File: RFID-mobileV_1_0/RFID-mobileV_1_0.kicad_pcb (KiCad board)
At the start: 2 copper layers, 50.7 x 89.5 mm, 54 parts, among them J1 USB_C_Receptacle_USB2.0, J2 Conn_01x05_Male, J3 Conn_01x05_Female, J4 Conn_01x05_Male, Q1 MMBT3904, SW1 SW_Push, U1 XC6206P332MR, U2 E22-400T22S, U3 STM32G030FxP, U4 LM321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

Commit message: pcb update
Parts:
- moved R13 31.9 mm to (66.3, 142.2), turned to 0 degrees
- moved D1 31.5 mm to (66.3, 144.3), turned to 180 degrees
- moved J4 19.1 mm to (102.6, 84.8), turned to -90 degrees
- moved AE1 3.22 mm to (82.7, 90.9)
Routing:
- net /RFID_RXD_: track 0.00 -> 63.5 mm
- net /RFID_TXD_: track 0.00 -> 61.2 mm
- net /ANT: track 12.2 -> 0.00 mm
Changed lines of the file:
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@@
   (net 55 "unconnected-(U5-Pad1)")
   (footprint "LED_SMD:LED_0805_2012Metric" (layer "F.Cu")
-    (at 90.424 123.952 90)
+    (at 66.294 144.272 180)
     (descr "LED SMD 0805 (2012 Metric), square (rectangular) end terminal, IPC_7351 nominal, (Body size source: https://docs.google.com/spreadsheets/d/1BsfQQcO9C6DZCsRaXUlFlo91Tg2WpOkGARC1WS5S8t0/edit?usp=sharing), generated with kicad-footprint-generator")
     (tags "LED")
@@
     (property "Sheetname" "")
     (attr smd)
-    (fp_text reference "D1" (at 0 -1.65 90) (layer "F.SilkS")
-      (effects (font (size 1 1) (thickness 0.15)))
-    )
-    (fp_text value "PWR" (at 0 1.65 90) (layer "F.Fab")
-      (effects (font (size 1 1) (thickness 0.15)))
-    )
-    (fp_text user "${REFERENCE}" (at 0 0 90) (layer "F.Fab")
+    (fp_text reference "D1" (at 0 -1.65) (layer "F.SilkS")
+      (effects (font (size 1 1) (thickness 0.15)))
+    )
+    (fp_text value "PWR" (at 0 1.65) (layer "F.Fab")
+      (effects (font (size 1 1) (thickness 0.15)))
+    )
+    (fp_text user "${REFERENCE}" (at 0 0) (layer "F.Fab")
       (effects (font (size 0.5 0.5) (thickness 0.08)))
     )
@@
     (fp_line (start 1 0.6) (end 1 -0.6) (layer "F.Fab") (width 0.1))
     (fp_line (start -1 -0.3) (end -1 0.6) (layer "F.Fab") (width 0.1))
-    (pad "1" smd roundrect (at -0.9375 0 90) (size 0.975 1.4) (layers "F.Cu" "F.Paste" "F.Mask") (roundrect_rratio 0.25)
+    (pad "1" smd roundrect (at -0.9375 0 180) (size 0.975 1.4) (layers "F.Cu" "F.Paste" "F.Mask") (roundrect_rratio 0.25)
       (net 7 "GND") (pinfunction "K") (pintype "passive"))
-    (pad "2" smd roundrect (at 0.9375 0 90) (size 0.975 1.4) (layers "F.Cu" "F.Paste" "F.Mask") (roundrect_rratio 0.25)
+    (pad "2" smd roundrect (at 0.9375 0 180) (size 0.975 1.4) (layers "F.Cu" "F.Paste" "F.Mask") (roundrect_rratio 0.25)
       (net 9 "Net-(D1-Pad2)") (pinfunction "A") (pintype "passive"))
     (model "${KICAD6_3DMODEL_DIR}/LED_SMD.3dshapes/LED_0805_2012Metric.wrl"
@@
   )
   (footprint "Resistor_SMD:R_0805_2012Metric" (layer "F.Cu")
-    (at 92.456 123.952 -90)
+    (at 66.294 142.24)
     (descr "Resistor SMD 0805 (2012 Metric), square (rectangular) end terminal, IPC_7351 nominal, (Body size source: IPC-SM-782 page 72, https://www.pcb-3d.com/wordpress/wp-content/uploads/ipc-sm-782a_amendment_1_and_2.pdf), generated with kicad-footprint-generator")
     (tags "resistor")
@@
     (property "Sheetname" "")
     (attr smd)
-    (fp_text reference "R13" (at 0 -1.65 90) (layer "F.SilkS")
-      (effects (font (size 1 1) (thickness 0.15)))
-    )
-    (fp_text value "330" (at 0 1.65 90) (layer "F.Fab")
-      (effects (font (size 1 1) (thickness 0.15)))
-    )
-    (fp_text user "${REFERENCE}" (at 0 0 90) (layer "F.Fab")
+    (fp_text reference "R13" (at 0 -1.65) (layer "F.SilkS")
+      (effects (font (size 1 1) (thickness 0.15)))
+    )
+    (fp_text value "330" (at 0 1.65) (layer "F.Fab")
+      (effects (font (size 1 1) (thickness 0.15)))
+    )
+    (fp_text user "${REFERENCE}" (at 0 0) (layer "F.Fab")
       (effects (font (size 0.5 0.5) (thickness 0.08)))
     )
@@
     (fp_line (start -1 -0.625) (end 1 -0.625) (layer "F.Fab") (width 0.1))
     (fp_line (start -1 0.625) (end -1 -0.625) (layer "F.Fab") (width 0.1))
-    (pad "1" smd roundrect (at -0.9125 0 270) (size 1.025 1.4) (layers "F.Cu" "F.Paste" "F.Mask") (roundrect_rratio 0.243902)
+    (pad "1" smd roundrect (at -0.9125 0) (size 1.025 1.4) (layers "F.Cu" "F.Paste" "F.Mask") (roundrect_rratio 0.243902)
       (net 9 "Net-(D1-Pad2)") (pintype "passive"))
-    (pad "2" smd roundrect (at 0.9125 0 270) (size 1.025 1.4) (layers "F.Cu" "F.Paste" "F.Mask") (roundrect_rratio 0.243902)
+    (pad "2" smd roundrect (at 0.9125 0) (size 1.025 1.4) (layers "F.Cu" "F.Paste" "F.Mask") (roundrect_rratio 0.243902)
       (net 4 "+3V3") (pintype "passive"))
     (model "${KICAD6_3DMODEL_DIR}/Resistor_SMD.3dshapes/R_0805_2012Metric.wrl"
@@
   )
   (footprint "Connector_PinHeader_2.54mm:PinHeader_1x05_P2.54mm_Vertical" (layer "F.Cu")
-    (at 83.566 83.82 90)
+    (at 102.611 84.836 -90)
     (descr "Through hole straight pin header, 1x05, 2.54mm pitch, single row")
     (tags "Through hole pin header THT 1x05 2.54mm single row")
@@
     (fp_line (start 1.27 -1.27) (end 1.27 11.43) (layer "F.Fab") (width 0.1))
     (fp_line (start -1.27 11.43) (end -1.27 -0.635) (layer "F.Fab") (width 0.1))
-    (pad "1" thru_hole rect (at 0 0 90) (size 1.7 1.7) (drill 1) (layers *.Cu *.Mask)
+    (pad "1" thru_hole rect (at 0 0 270) (size 1.7 1.7) (drill 1) (layers *.Cu *.Mask)
       (net 4 "+3V3") (pinfunction "Pin_1") (pintype "passive"))
-    (pad "2" thru_hole oval (at 0 2.54 90) (size 1.7 1.7) (drill 1) (layers *.Cu *.Mask)
+    (pad "2" thru_hole oval (at 0 2.54 270) (size 1.7 1.7) (drill 1) (layers *.Cu *.Mask)
       (net 29 "/RFID_TXD_") (pinfunction "Pin_2") (pintype "passive"))
-    (pad "3" thru_hole oval (at 0 5.08 90) (size 1.7 1.7) (drill 1) (layers *.Cu *.Mask)
+    (pad "3" thru_hole oval (at 0 5.08 270) (size 1.7 1.7) (drill 1) (layers *.Cu *.Mask)
       (net 30 "/RFID_RXD_") (pinfunction "Pin_3") (pintype "passive"))
-    (pad "4" thru_hole oval (at 0 7.62 90) (size 1.7 1.7) (drill 1) (layers *.Cu *.Mask)
+    (pad "4" thru_hole oval (at 0 7.62 270) (size 1.7 1.7) (drill 1) (layers *.Cu *.Mask)
       (net 31 "unconnected-(J4-Pad4)") (pinfunction "Pin_4") (pintype "passive+no_connect"))
-    (pad "5" thru_hole oval (at 0 10.16 90) (size 1.7 1.7) (drill 1) (layers *.Cu *.Mask)
+    (pad "5" thru_hole oval (at 0 10.16 270) (size 1.7 1.7) (drill 1) (layers *.Cu *.Mask)
       (net 7 "GND") (pinfunction "Pin_5") (pintype "passive"))
     (model "${KICAD6_3DMODEL_DIR}/Connector_PinHeader_2.54mm.3dshapes/PinHeader_1x05_P2.54mm_Vertical.wrl"
@@
   )
   (footprint "RF_Antenna:433MHz" (layer "F.Cu")
-    (at 85.852 91.44 180)
+    (at 82.677 90.932001 180)
     (property "Sheetfile" "RFID-mobileV_1_0.kicad_sch")
     (property "Sheetname" "")
@@
   (gr_arc locked (start 66.16277 161.39279) (mid 64.73449 161.282141) (end 64.050435 160.023467) (layer "Edge.Cuts") (width 0.2))
   (gr_circle locked (center 110.407996 100.913642) (end 113.407996 100.913642) (layer "Edge.Cuts") (width 0.2) (fill none))
-  (segment (start 75.692 95.943) (end 75.692 89.154) (width 0.25) (layer "F.Cu") (net 1))
-  (segment (start 75.692 89.154) (end 76.2 88.646) (width 0.25) (layer "F.Cu") (net 1))
-  (segment (start 77.016 97.267) (end 75.692 95.943) (width 0.25) (layer "F.Cu") (net 1))
-  (segment (start 77.016 98.417) (end 77.016 97.267) (width 0.25) (layer "F.Cu") (net 1))
-  (segment (start 76.708 88.646) (end 77.0265 88.9645) (width 0.25) (layer "F.Cu") (net 1))
-  (segment (start 76.2 88.646) (end 76.708 88.646) (width 0.25) (layer "F.Cu") (net 1))
-  (segment (start 77.0265 88.9645) (end 77.0265 89.662) (width 0.25) (layer "F.Cu") (net 1))
   (segment (start 77.216 140.97) (end 79.455 140.97) (width 0.6) (layer "F.Cu") (net 2))
   (segment (start 79.484 140.941) (end 79.455 140.97) (width 0.6) (layer "F.Cu") (net 2))
@@
   (segment (start 101.092 132.842) (end 102.616 134.366) (width 0.25) (layer "F.Cu") (net 28))
   (segment (start 102.616 134.366) (end 102.616 136.144) (width 0.25) (layer "F.Cu") (net 28))
+  (segment (start 105.918 133.35) (end 105.918 113.03) (width 0.25) (layer "F.Cu") (net 29))
+  (segment (start 108.966 111.506) (end 102.616 111.506) (width 0.25) (layer "F.Cu") (net 29))
+  (segment (start 102.616 111.506) (end 100.66256 109.55256) (width 0.25) (layer "F.Cu") (net 29))
+  (segment (start 100.071 94.355282) (end 100.071 84.836) (width 0.25) (layer "F.Cu") (net 29))
+  (segment (start 104.7165 136.013) (end 104.7165 134.5515) (width 0.25) (layer "F.Cu") (net 29))
+  (segment (start 100.66256 94.946842) (end 100.071 94.355282) (width 0.25) (layer "F.Cu") (net 29))
+  (segment (start 105.918 113.03) (end 107.442 111.506) (width 0.25) (layer "F.Cu") (net 29))
+  (segment (start 107.442 111.506) (end 108.966 111.506) (width 0.25) (layer "F.Cu") (net 29))
+  (segment (start 100.66256 109.55256) (end 100.66256 94.946842) (width 0.25) (layer "F.Cu") (net 29))
+  (segment (start 104.7165 134.5515) (end 105.918 133.35) (width 0.25) (layer "F.Cu") (net 29))
+  (segment (start 91.44 134.112) (end 90.05304 132.72504) (width 0.25) (layer "F.Cu") (net 30))
+  (segment (start 90.05304 132.334) (end 100.21304 122.174) (width 0.25) (layer "F.Cu") (net 30))
+  (segment (start 90.05304 132.72504) (end 90.05304 132.334) (width 0.25) (layer "F.Cu") (net 30))
+  (segment (start 100.21304 95.13304) (end 97.531 92.451) (width 0.25) (layer "F.Cu") (net 30))
+  (segment (start 97.0905 134.112) (end 93.726 134.112) (width 0.25) (layer "F.Cu") (net 30))
+  (segment (start 100.21304 122.174) (end 100.21304 120.903999) (width 0.25) (layer "F.Cu") (net 30))
+  (segment (start 93.726 134.112) (end 91.44 134.112) (width 0.25) (layer "F.Cu") (net 30))
+  (segment (start 98.9915 136.013) (end 97.0905 134.112) (width 0.25) (layer "F.Cu") (net 30))
+  (segment (start 97.531 92.451) (end 97.531 84.836) (width 0.25) (layer "F.Cu") (net 30))
+  (segment (start 100.21304 120.903999) (end 100.21304 95.13304) (width 0.25) (layer "F.Cu") (net 30))
   (segment (start 90.756 113.616) (end 88.138 110.998) (width 0.25) (layer "F.Cu") (net 32))
   (segment (start 90.756 114.417) (end 90.756 113.616) (width 0.25) (layer "F.Cu") (net 32))

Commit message: update
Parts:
- AE1: footprint RF_Antenna:433MHz -> RF_Antenna:433MHz_V
- moved R12 19.5 mm to (79.8, 158.5)
- moved C2 18.6 mm to (96.3, 158.0)
- moved C1 18.6 mm to (99.1, 155.2)
- moved U1 18.6 mm to (99.3, 158.0)
- moved U5 18.2 mm to (84.8, 153.9)
- moved J3 13.5 mm to (103.1, 122.2), turned to 0 degrees
- moved C6 11.9 mm to (76.2, 145.0), turned to 90 degrees
- moved BT1 11.8 mm to (78.2, 153.9), turned to 0 degrees
- moved R7 7.55 mm to (79.7, 148.5), turned to 90 degrees
- moved J4 7.27 mm to (104.1, 91.9), turned to 0 degrees
- moved R17 5.99 mm to (88.9, 153.2), turned to 180 degrees
- moved U4 5.85 mm to (79.5, 145.0), turned to 180 degrees
- moved R8 5.64 mm to (81.7, 148.5), turned to -90 degrees
- moved AE1 2.22 mm to (84.8, 90.4)
- moved R11 1.78 mm to (98.6, 164.8), turned to 0 degrees
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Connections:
- D2 pad 1: /PA6 -> /PA8
- D3 pad 1: /PA7 -> /PA9
- D4 pad 1: /PA8 -> /PA10
- U3 pad 12: /VBUS_sing -> /buz
- U3 pad 13: /PA6 -> /VBUS_sing
- U3 pad 16: unconnected-(U3-Pad16) -> /PA9
- U3 pad 17: unconnected-(U3-Pad17) -> /PA10
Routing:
- net +3V3: track 20.7 -> 280.1 mm, vias 0 -> 6
- net +BATT: track 5.78 -> 110.1 mm
- net /buz: track 0.00 -> 81.4 mm
- net /VBUS_sing: track 0.00 -> 45.0 mm
- net /CHAR_STAT: track 0.00 -> 35.8 mm, vias 0 -> 2
- net +5V: track 0.00 -> 33.1 mm
- net /BATT_moint: track 0.00 -> 30.8 mm, vias 0 -> 2
- net /RFID_TXD_: track 61.2 -> 46.2 mm
- net /PA6: track 13.1 -> 0.00 mm
- net /PA9: track 0.00 -> 10.4 mm, vias 0 -> 2
- net /PA7: track 9.93 -> 0.00 mm, vias 2 -> 0
- net /PA10: track 0.00 -> 9.08 mm, vias 0 -> 2
- net /RFID_RXD_: track 63.5 -> 54.9 mm
- net /CC1: track 0.00 -> 8.49 mm
- net /CC2: track 0.00 -> 7.78 mm
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- added copper zone on B.Cu, net GND
- added copper zone on F.Cu, net GND

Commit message: update
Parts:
- moved Q1 2.05 mm to (68.8, 118.1)
- moved R5 2.05 mm to (68.8, 115.1)
- moved R6 2.05 mm to (72.6, 118.1)
- moved R11 1.78 mm to (96.8, 164.8), turned to 180 degrees
- moved J1 0.73 mm to (89.4, 166.4)
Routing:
- net /NRST: track 40.1 -> 47.3 mm
- net GND: track 2.54 -> 8.11 mm
- net +5V: track 33.1 -> 36.4 mm
- net +3V3: track 280.1 -> 278.8 mm

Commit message: update
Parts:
- moved AE1 0.22 mm to (85.0, 90.6)
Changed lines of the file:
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@@
   )
   (footprint "RF_Antenna:433MHz_V" (layer "F.Cu")
-    (at 84.836 90.424 180)
+    (at 84.963 90.6018 180)
     (property "Sheetfile" "RFID-mobileV_1_0.kicad_sch")
     (property "Sheetname" "")
@@
   (gr_arc locked (start 66.16277 161.39279) (mid 64.73449 161.282141) (end 64.050435 160.023467) (layer "Edge.Cuts") (width 0.2))
   (gr_circle locked (center 110.407996 100.913642) (end 113.407996 100.913642) (layer "Edge.Cuts") (width 0.2) (fill none))
-  (segment (start 77.016 91.494) (end 77.016 98.417) (width 0.25) (layer "F.Cu") (net 1))
-  (segment (start 76.8975 91.186) (end 76.8975 91.3755) (width 0.25) (layer "F.Cu") (net 1))
-  (segment (start 76.8975 91.3755) (end 77.016 91.494) (width 0.25) (layer "F.Cu") (net 1))
+  (segment (start 77.016 91.3723) (end 77.016 98.417) (width 0.25) (layer "F.Cu") (net 1))
+  (segment (start 77.0245 91.3638) (end 77.016 91.3723) (width 0.25) (layer "F.Cu") (net 1))
   (segment (start 78.867 158.4995) (end 78.867 160.401) (width 0.6) (layer "F.Cu") (net 2))
   (segment (start 74.102 145.984) (end 76.2 145.984) (width 0.6) (layer "F.Cu") (net 2))

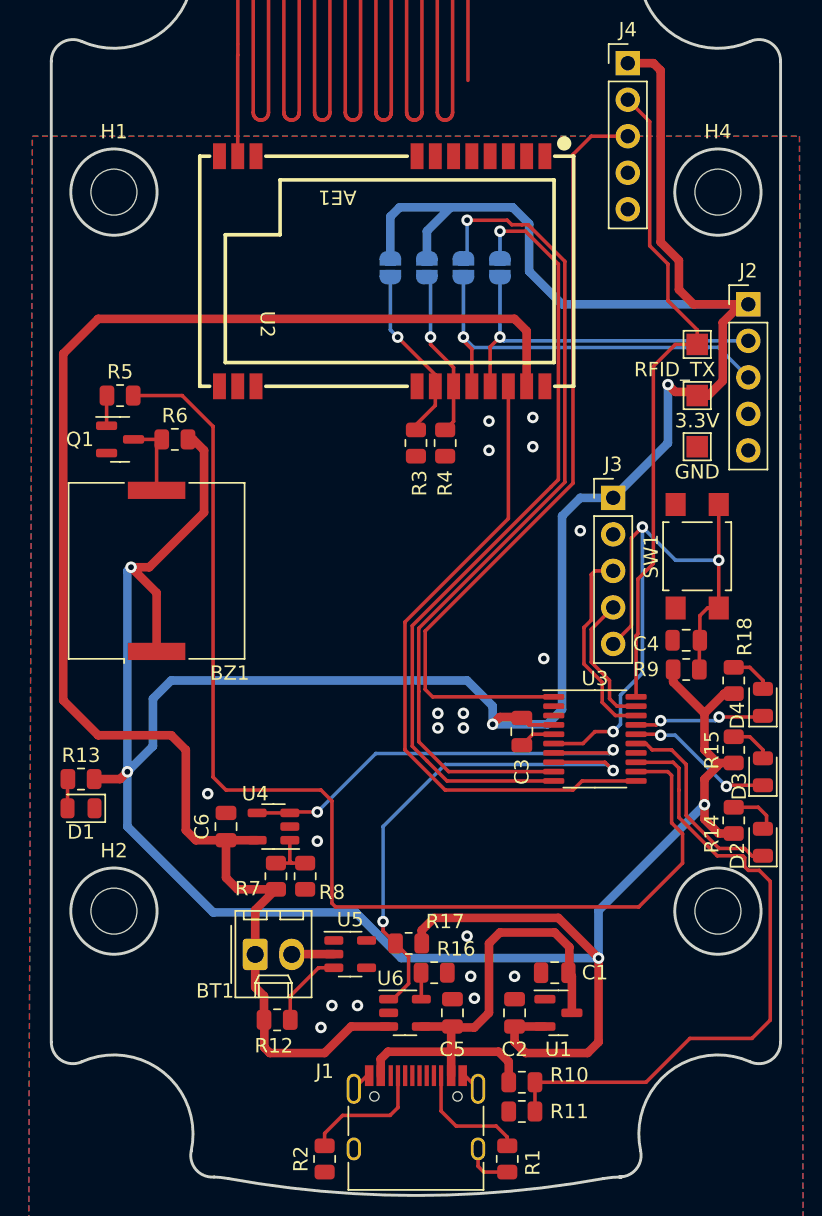
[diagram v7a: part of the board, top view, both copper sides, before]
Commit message: Update RFID-mobileV_1_0.kicad_pcb
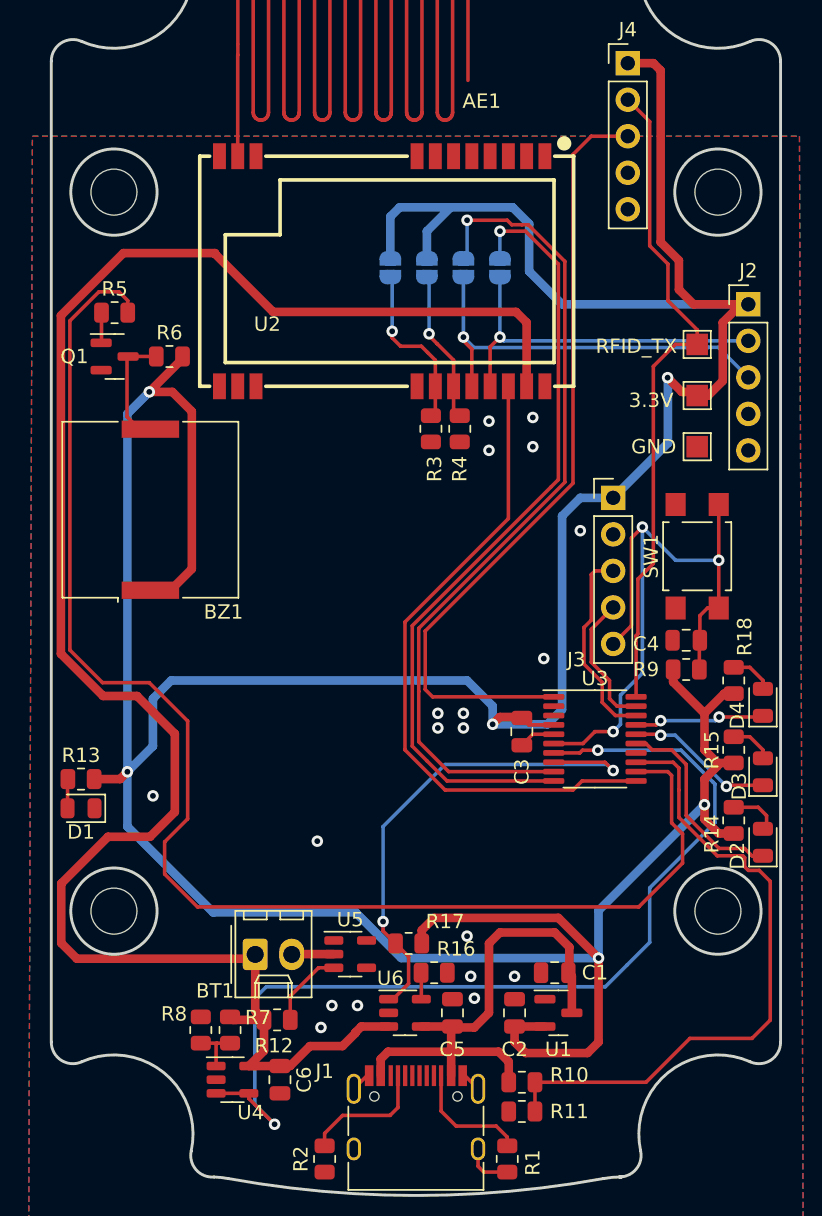
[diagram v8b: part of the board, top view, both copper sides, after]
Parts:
- moved C6 18.0 mm to (80.0, 162.6), turned to -90 degrees
- moved U4 17.8 mm to (76.6, 162.6), turned to 0 degrees
- moved R8 12.9 mm to (74.4, 159.2), turned to 90 degrees
- moved R7 11.2 mm to (76.5, 159.2), turned to -90 degrees
- moved Q1 5.78 mm to (68.5, 112.3)
- moved R5 5.78 mm to (68.5, 109.3)
- moved R6 5.78 mm to (72.3, 112.3)
- moved BZ1 4.28 mm to (70.9, 123.0)
- moved R3 1.44 mm to (90.4, 117.4)
- moved R4 1.42 mm to (92.5, 117.4)
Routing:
- net /BATT_moint: track 30.8 -> 68.7 mm
- net +BATT: track 110.1 -> 129.8 mm
- net /buz: track 81.6 -> 97.6 mm
- net +3V3: track 278.8 -> 294.6 mm
- net Net-(BZ1-Pad2): track 5.65 -> 8.17 mm
- net /M1: track 11.6 -> 10.6 mm
- net /M0: track 12.5 -> 11.9 mm
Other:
- board text added: "JP1:M0 JP2:M1 JP3:LoRa RX JP4:Lora TX"
